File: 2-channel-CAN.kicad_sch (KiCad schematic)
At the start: 32 parts, among them J3 Conn_01x02_Pin, J4 Conn_01x02_Pin, U10 B0505S-1WR3, U11 TC2185-3.3VxCTTR, U3 MCP2515-xSO, U6 MCP2515-xSO, U7 SN65HVD230, U8 SN65HVD230, U9 Si8642ED-B-IS, Y1 8MHz, Y2 8MHz

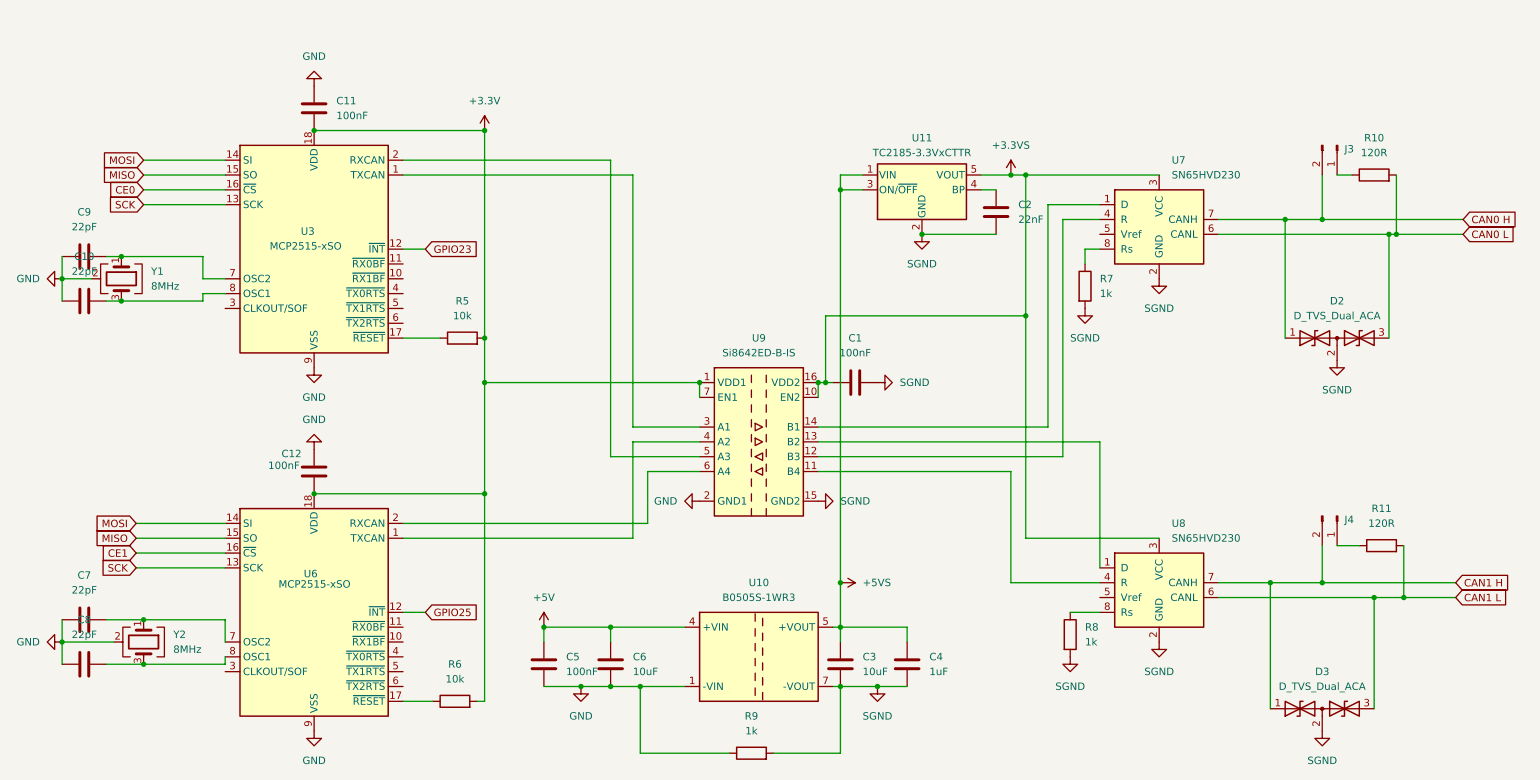
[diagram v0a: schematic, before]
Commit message: Remove non-existent security fields from bluer characteristics
The bluer crate's CharacteristicWrite and CharacteristicNotify
don't have encrypt_*/secure_* fields - removed them.

Co-Authored-By: Claude Opus 4.5 <noreply@anthropic.com>
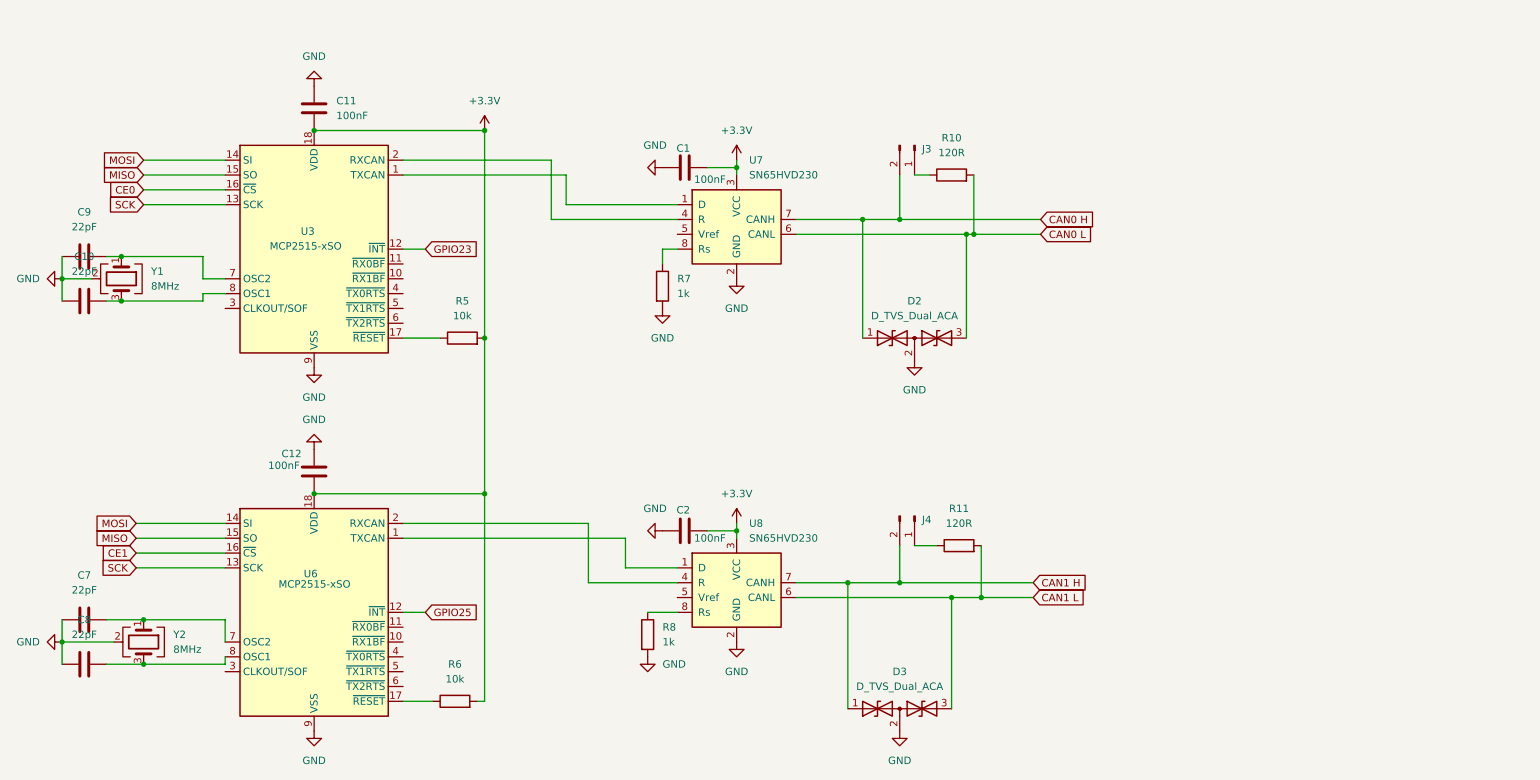
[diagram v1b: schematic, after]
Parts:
- removed C3, C6: 10uF, Capacitor_SMD:C_0402_1005Metric, symbol Device:C
- removed C4: 1uF, Capacitor_SMD:C_0402_1005Metric, symbol Device:C
- removed C5: 100nF, Capacitor_SMD:C_0402_1005Metric, symbol Device:C
- removed R9: 1k, Resistor_SMD:R_0402_1005Metric, symbol Device:R
- removed U10: B0505S-1WR3, Resistor_THT:R_Array_SIP4, symbol Regulator_Switching:CRE1S0505DC
- removed U11: TC2185-3.3VxCTTR, Package_TO_SOT_SMD:SOT-23-5, symbol Regulator_Linear:TC2185-3.3VxCTTR
- removed U9: Si8642ED-B-IS, Package_SO:SOIC-16W_7.5x10.3mm_P1.27mm, symbol Isolator:Si8642ED-B-IS
- C2: value 22nF -> 100nF
- D2, D3: footprint (none) -> Package_TO_SOT_SMD:SOT-23
- J3, J4: now left out of the parts list
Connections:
- net +3.3VS is gone; now on net +3.3V: C1.1, U7.3 (VCC), U8.3 (VCC)
- net SGND is gone; now on net GND: C1.2, C2.2, D2.2 (common), D3.2 (common), R7.2, R8.2, U7.2 (GND), U8.2 (GND)
- net +3.3V: now also C2.1
- net at U6.1 (TXCAN): now also U8.1 (D)
- net at U6.2 (RXCAN): now also U8.4 (R)
- net at U7.4 (R): now also U3.2 (RXCAN)
- net at U7.1 (D): now also U3.1 (TXCAN)
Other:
- moved on the sheet: C1, D2, D3, J3, J4, R10, R11, R7, R8, U7, U8

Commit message: Rename project to Perfect-Vision-ECU
- Rename main project files from Raspberry-Pi-Backup-power-and-GPS-hat-v4
- Update relay footprint to G6K-2F-Y to match LCSC part C397194
- Update C4 capacitor to CP_Elec_8x10.5 with LCSC C3353 (220uF 25V)
- Add new power supply schematic
- Update JLCPCB production files (gerbers, BOM, CPL)
- Remove old firmware and Raspberry Pi specific files

Co-Authored-By: Claude Opus 4.5 <noreply@anthropic.com>
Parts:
- removed C10, C9: 22pF, Capacitor_SMD:C_0402_1005Metric, symbol Device:C
- removed C11: 100nF, Capacitor_SMD:C_0402_1005Metric, symbol Device:C
- removed J3, J4: Conn_01x02_Pin, Connector_PinHeader_2.54mm:PinHeader_1x02_P2.54mm_Vertical, symbol Connector:Conn_01x02_Pin
- removed R10, R11: 120R, Resistor_SMD:R_0402_1005Metric, symbol Device:R
- removed U3: MCP2515-xSO, Package_SO:SOIC-18W_7.5x11.6mm_P1.27mm, symbol Interface_CAN_LIN:MCP2515-xSO
- removed Y1: 8MHz, Crystal:Crystal_SMD_3225-4Pin_3.2x2.5mm, symbol Device:Crystal_GND24
- added D10: 1N4148W, Diode_SMD:D_SOD-123, symbol Diode:1N4148W
- added D11: LED, LED_SMD:LED_0603_1608Metric, symbol Device:LED
- added K1: G6K-2 12V, Relay_SMD:Relay_DPDT_Omron_G6K-2F-Y, symbol Relay:G6K-2
- added Q1: PZT2222A, Package_TO_SOT_SMD:SOT-223-3_TabPin2, symbol Transistor_BJT:PZT2222A
- added R2: 120R, Resistor_SMD:R_0402_1005Metric, symbol Device:R
- added R9: 1k, Resistor_SMD:R_0402_1005Metric, symbol Device:R
- R5: value 10k -> 1k
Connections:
- net +3.3V: no longer R5.2
- net GND: now also Q1.3 (E)
- net IO8_RELAY: now reaches R5.1
- net IO5: now reaches U7.1 (D)
- net IO4: now reaches U7.4 (R)
- net CAN0 H renamed CAN1_H_IMPL
- net CAN1_H_IMPL: now also K1.3
- net CAN0 L renamed CAN1_L_IMPL
- net CAN1_L_IMPL: now also K1.6
- net CE1 renamed CS
- net GPIO25 renamed IO9
- new net: D10.2 (A), D11.1 (K), K1.1, Q1.2 (C)
- new net: D11.2 (A), R9.1
- new net: K1.4, R2.1
- new net: K1.5, R2.2
- new net: Q1.1 (B), R5.2
- new net +12V: D10.1 (K), K1.8, R9.2
- new net CAN1_H_TRACTOR: K1.2
- new net CAN1_L_TRACTOR: K1.7
